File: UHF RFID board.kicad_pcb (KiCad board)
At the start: 2 copper layers, 67.3 x 36.7 mm, 34 parts, among them J1 FZ_full_module, J2 picoblade, J3 SPI, J4 ICSP, U1 YRM1001, U2 SEC1210

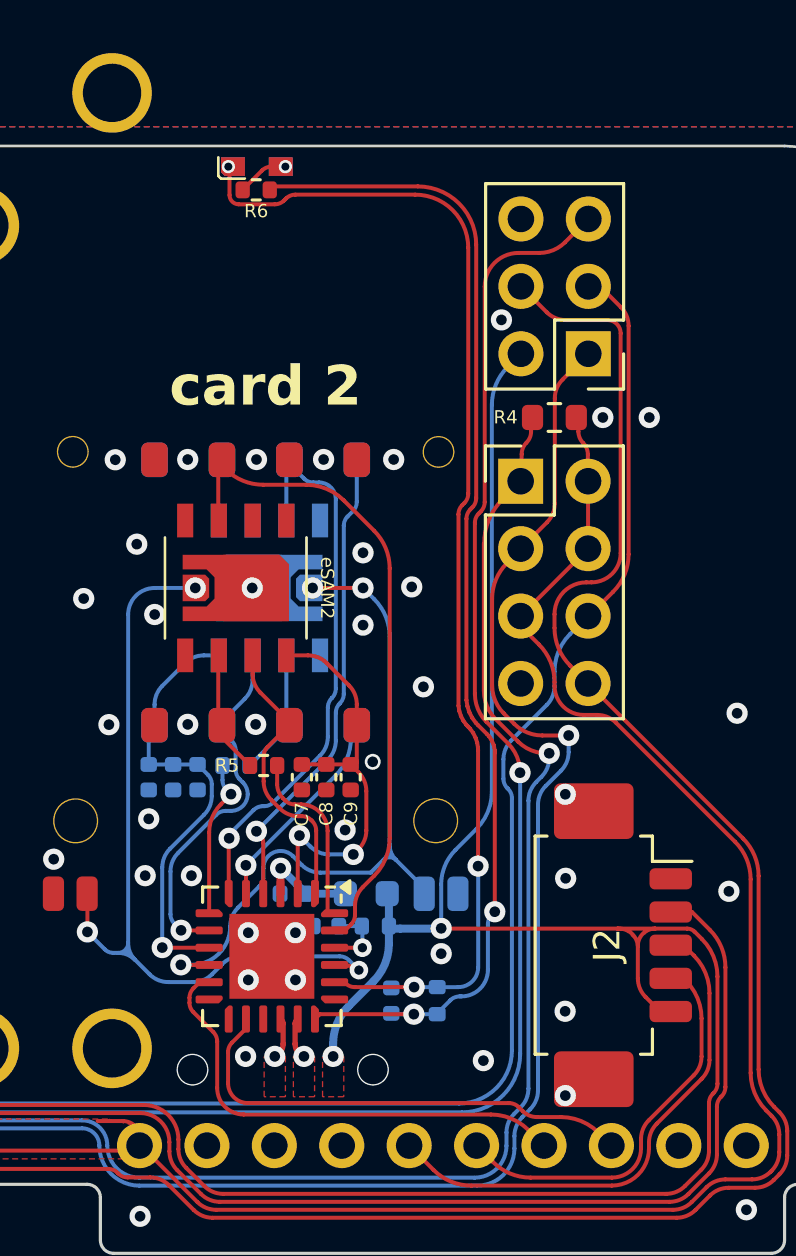
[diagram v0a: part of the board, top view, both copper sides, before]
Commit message: removed no longer needed features (LEDs, USB)
After testing it turns out the USB port on the SEC1210 UART version does not seem to be enabled. Therefore there's no way to program the chip to enable the LED output.
Removed unneeded D1, D2, R6, and re-positioned R1 and C1 thanks to the extra space.
updated schematic with DNP tags for D1, D2, R6.
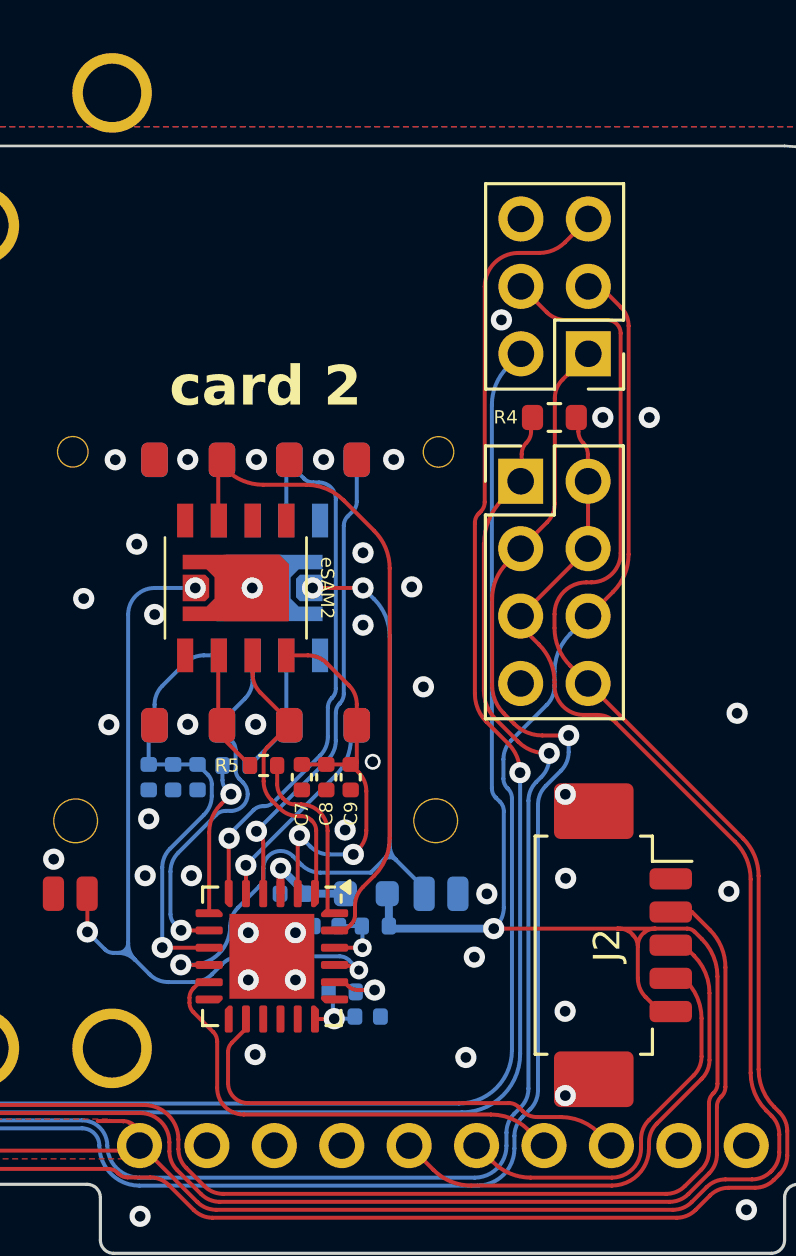
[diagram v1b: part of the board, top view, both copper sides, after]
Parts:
- removed D1: LED, Custom LEDs:kingbright AGPA1602
- removed D2: LED, Custom LEDs:kingbright AGPA1602 - FLIPPED
- removed R6: 33R, Resistor_SMD:R_0402_1005Metric
- moved R1 3.60 mm to (166.0, 127.5), turned to 180 degrees
- moved C1 1.07 mm to (167.0, 128.4), turned to 0 degrees
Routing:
- net +3.3VA: track 45.1 -> 2.64 mm, vias 2 -> 1
- net /LED_ACT: track 44.9 -> 2.58 mm, vias 3 -> 1
- net +5V: track 115.1 -> 109.2 mm, vias 2 -> 1
- net Net-(D1-A): track 1.77 -> 0.00 mm, vias 1 -> 0
- net /USB_DP: track 1.58 -> 0.00 mm, vias 1 -> 0
- net /USB_DN: track 1.58 -> 0.00 mm, vias 1 -> 0
- net GND: vias 97 -> 96
- removed copper zone on F.Cu, net /USB_DN
- removed copper zone on F.Cu, net /USB_DP
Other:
- board text added: "UHF | RFID | SAM Version 2.4"
- board text removed: "+5V"
- board text removed: "D+"
- board text removed: "D-"
- board text removed: "GND"
- board text removed: "UHF | RFID | SAM Version 2.3"

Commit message: futureproofing for automated production
Added fiducial markers for automated PNP machine assembly capability.
updated version from 2.4 to 2.5
added version info in schematic, along with title and my name for credit
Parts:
- added ?: , , F.Cu at (122.2, 136.5)
- added ?: , , F.Cu at (181.9, 136.5)
- added ?: , , B.Cu at (136.9, 101.6)
- added ?: , , B.Cu at (122.2, 136.5)
- added ?: , , B.Cu at (181.9, 136.5)
- added ?: , , B.Cu at (177.9, 98.3)
- added ?: , , B.Cu at (136.9, 126.6)
- added ?: , , B.Cu at (124.4, 114.1)
- added ?: , , B.Cu at (149.4, 114.1)
- added REF**: Fiducial_0.5mm_Mask1mm, Fiducial:Fiducial_0.5mm_Mask1mm, F.Cu at (149.4, 114.1)
- added REF**: Fiducial_0.5mm_Mask1mm, Fiducial:Fiducial_0.5mm_Mask1mm, F.Cu at (177.9, 98.3)
- added REF**: Fiducial_0.5mm_Mask1mm, Fiducial:Fiducial_0.5mm_Mask1mm, F.Cu at (136.9, 101.6)
- added REF**: Fiducial_0.5mm_Mask1mm, Fiducial:Fiducial_0.5mm_Mask1mm, F.Cu at (136.9, 126.6)
- added REF**: Fiducial_0.5mm_Mask1mm, Fiducial:Fiducial_0.5mm_Mask1mm, F.Cu at (124.4, 114.1)
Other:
- board text added: "UHF | RFID | SAM Version 2.5"
- board text added: "UHF-RFID_SAM-interface_Board/"
- board text removed: "UHF | RFID | SAM Version 2.4"
